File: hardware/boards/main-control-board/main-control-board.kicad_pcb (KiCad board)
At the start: 2 copper layers, 122.9 x 33 mm, 7 parts, among them J1 Conn_MAX98357, J2 Conn_OLED, J3 Conn_PCA9685_1, J4 Conn_PCA9685_2, J5 Conn_ESP32_R, J6 Conn_ESP32_L, J7 Conn_USB

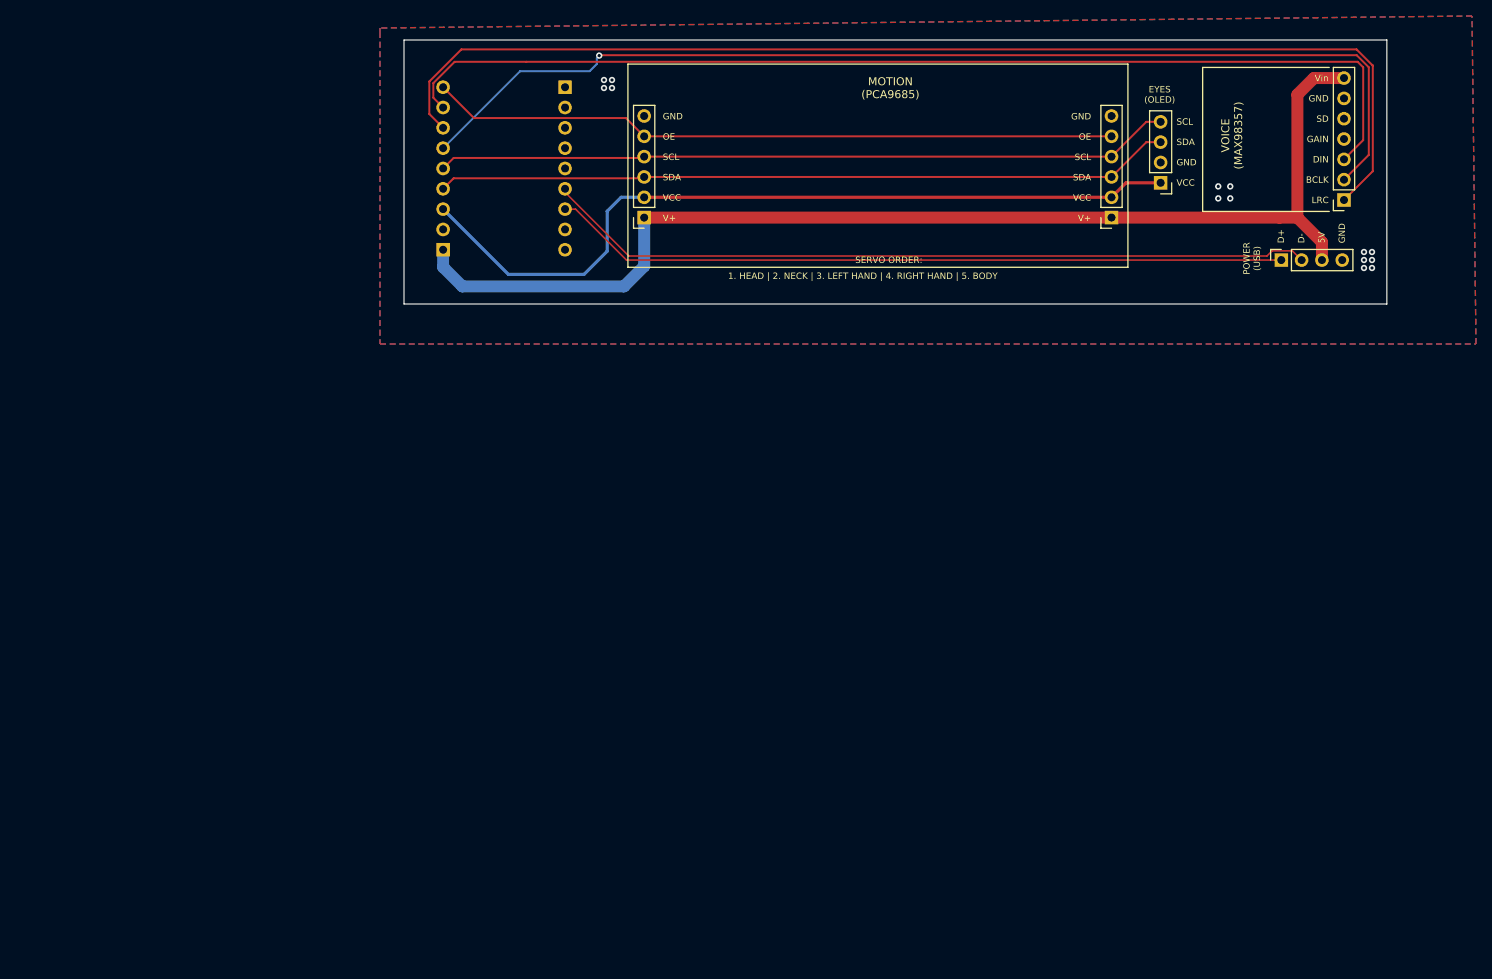
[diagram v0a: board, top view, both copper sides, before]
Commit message: reshape the board to mount SDM USB
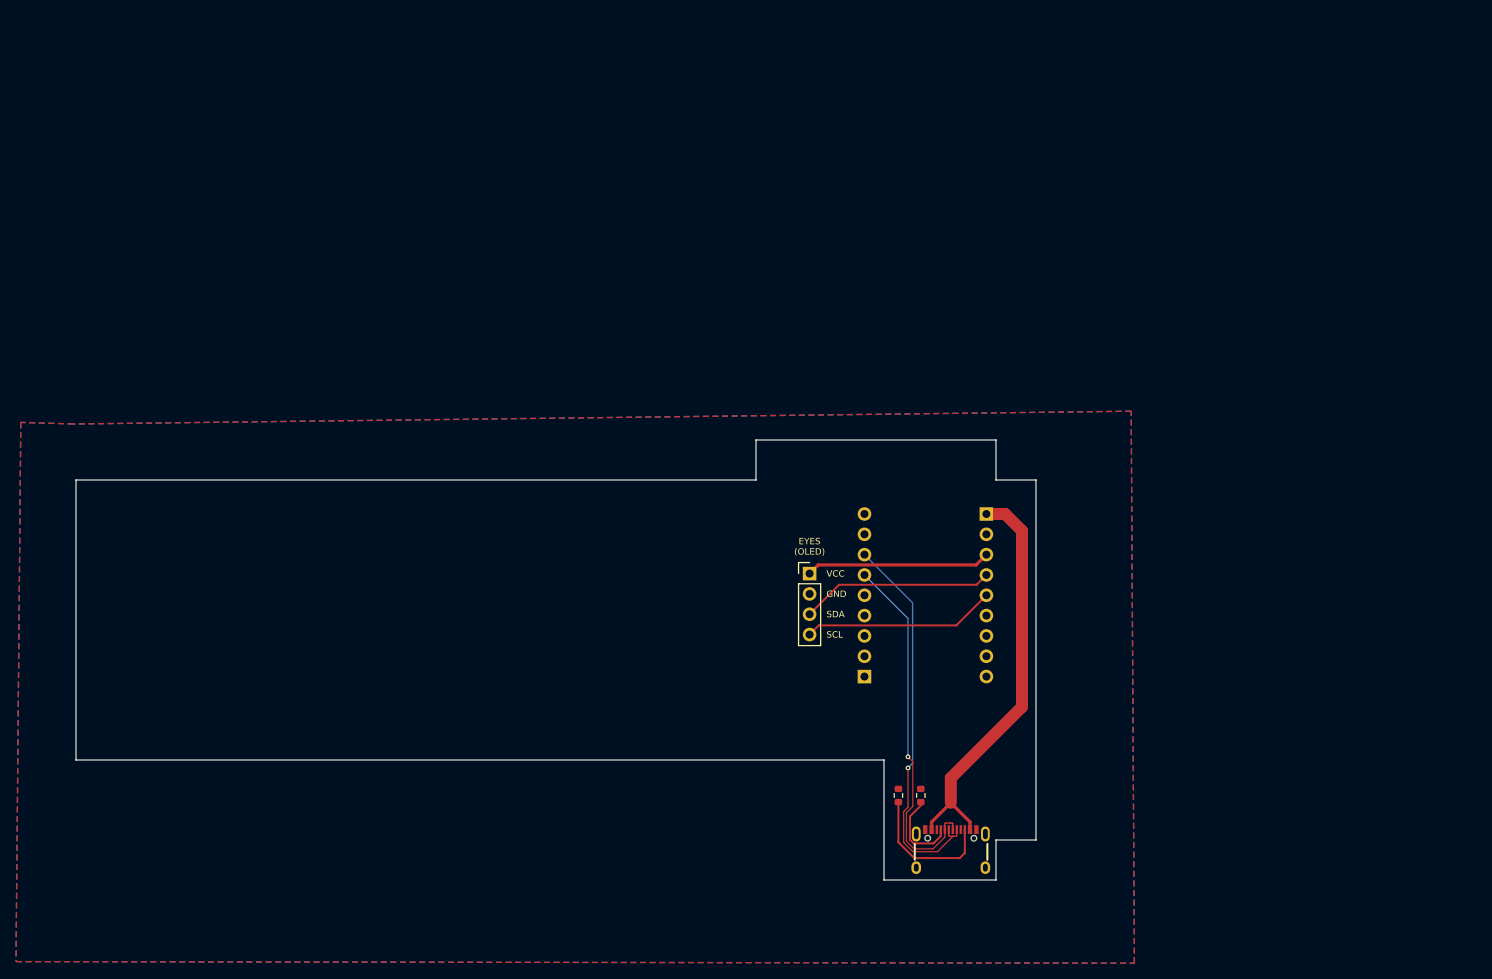
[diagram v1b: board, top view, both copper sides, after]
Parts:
- removed J1: Conn_MAX98357, Connector_PinSocket_2.54mm:PinSocket_1x07_P2.54mm_Vertical
- removed J3: Conn_PCA9685_1, Connector_PinSocket_2.54mm:PinSocket_1x06_P2.54mm_Vertical
- removed J4: Conn_PCA9685_2, Connector_PinSocket_2.54mm:PinSocket_1x06_P2.54mm_Vertical
- removed J7: Conn_USB, Connector_PinSocket_2.54mm:PinSocket_1x04_P2.54mm_Vertical
- added R1: 5.1k, Resistor_SMD:R_0603_1608Metric, F.Cu at (188.1, 124.4)
- added R2: 5.1k, Resistor_SMD:R_0603_1608Metric, F.Cu at (185.3, 124.4)
- added USB1: TYPE-C 16PIN 2MD, easyeda:USB-C-SMD_TYPE-C-16PIN-2MD-073, F.Cu at (191.8, 131.1)
- moved J5 82.6 mm to (181.1, 109.6), turned to 0 degrees
- moved J6 75.5 mm to (196.3, 89.2), turned to 180 degrees
- moved J2 65.7 mm to (174.2, 96.7), turned to 0 degrees
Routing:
- net /I2S_LRC: track 145.2 -> 0.00 mm
- net /I2S_BCLK: track 136.9 -> 0.00 mm, vias 1 -> 0
- net /I2S_DIN: track 133.7 -> 0.00 mm
- net +5V: track 145.7 -> 51.7 mm
- net Net-(J3-Pin_5): track 86.1 -> 0.00 mm
- net +3.3V: track 101.0 -> 23.1 mm
- net /I2C_SCL: track 92.2 -> 24.1 mm
- net /I2C_SDA: track 92.1 -> 24.1 mm
- net /USB_D-: track 96.5 -> 45.4 mm, vias 0 -> 1
- net /USB_D+: track 92.2 -> 48.9 mm, vias 0 -> 1
- net Net-(USB1-CC2): track 0.00 -> 17.3 mm
- net Net-(USB1-CC1): track 0.00 -> 10.5 mm
- net GND: vias 14 -> 0
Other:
- board size 122.9 x 33 mm -> 120 x 55 mm
- board text removed: "1. HEAD | 2. NECK | 3. LEFT HAND | 4. RIGHT HAND | 5. BODY"
- board text removed: "BCLK"
- board text removed: "D+"
- board text removed: "D-"
- board text removed: "DIN"
- board text removed: "GAIN"
- board text removed: "LRC"
- board text removed: "MOTION (PCA9685)"
- board text removed: "OE"
- board text removed: "POWER (USB)"
- board text removed: "SD"
- board text removed: "SERVO ORDER:"
- board text removed: "V+"
- board text removed: "VOICE (MAX98357)"
- board text removed: "Vin"

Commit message: use hierarchical sheets in schmatic
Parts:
- removed J5: Conn_ESP32_R, Connector_PinSocket_2.54mm:PinSocket_1x09_P2.54mm_Vertical
- removed J6: Conn_ESP32_L, Connector_PinSocket_2.54mm:PinSocket_1x09_P2.54mm_Vertical
- added J7: Conn_ESP32_L, Connector_PinSocket_2.54mm:PinSocket_1x09_P2.54mm_Vertical, B.Cu at (196.3, 89.3)
- added J8: Conn_ESP32_R, Connector_PinSocket_2.54mm:PinSocket_1x09_P2.54mm_Vertical, B.Cu at (181.1, 109.6)
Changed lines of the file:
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@@
 			)
 		)
-		(sheetname "/")
-		(sheetfile "main-control-board.kicad_sch")
+		(sheetname "/USB/")
+		(sheetfile "main-control-board-usb.kicad_sch")
+		(units
+			(unit
+				(name "A")
+				(pins "A1B12" "A4B9" "B8" "A5" "B7" "A6" "A7" "B6" "A8" "B5" "B4A9" "B1A12"
+					"13" "14"
+				)
+			)
+		)
 		(attr smd)
 		(duplicate_pad_numbers_are_jumpers no)
@@
 			)
 		)
-		(property "KiLib_Generator" "SMD_2terminal_chip_molded"
-			(at 0 0 90)
-			(layer "F.SilkS")
-			(hide yes)
-			(effects
-				(font
-					(size 1 1)
-					(thickness 0.15)
-				)
-			)
-		)
 		(property "LCSC Part #" "C23186"
 			(at 0 0 270)
@@
 		)
 		(property ki_fp_filters "R_*")
-		(sheetname "/")
-		(sheetfile "main-control-board.kicad_sch")
+		(sheetname "/USB/")
+		(sheetfile "main-control-board-usb.kicad_sch")
 		(units
 			(unit
@@
 			)
 		)
-		(property "KiLib_Generator" "SMD_2terminal_chip_molded"
-			(at 0 0 90)
-			(layer "F.SilkS")
-			(hide yes)
-			(effects
-				(font
-					(size 1 1)
-					(thickness 0.15)
-				)
-			)
-		)
 		(property "LCSC Part #" "C23186"
 			(at 0 0 270)
@@
 		)
 		(property ki_fp_filters "R_*")
-		(sheetname "/")
-		(sheetfile "main-control-board.kicad_sch")
+		(sheetname "/USB/")
+		(sheetfile "main-control-board-usb.kicad_sch")
 		(units
 			(unit
@@
 	)
 	(footprint "Connector_PinSocket_2.54mm:PinSocket_1x09_P2.54mm_Vertical"
+		(locked yes)
 		(layer "B.Cu")
-		(at 196.3 89.25 180)
+		(at 196.3 89.28 180)
 		(descr "Through hole straight socket strip, 1x09, 2.54mm pitch, single row (from Kicad 4.0.7), script generated")
 		(tags "Through hole socket strip THT 1x09 2.54mm single row")
-		(property "Reference" "J6"
+		(property "Reference" "J7"
 			(at 0 2.77 0)
 			(layer "B.SilkS")
@@
 			(at 0 -23.09 0)
 			(layer "B.Fab")
-			(hide yes)
 			(effects
 				(font
@@
 				(font
 					(size 1.27 1.27)
-				)
-				(justify mirror)
-			)
-		)
-		(property "KiLib_Generator" "connector/pin_header_socket"
-			(at 0 0 0)
-			(layer "B.SilkS")
-			(hide yes)
-			(effects
-				(font
-					(size 1 1)
-					(thickness 0.15)
 				)
 				(justify mirror)
@@
 		)
 		(property ki_fp_filters "Connector*:*_1x??_*")
-		(sheetname "/")
-		(sheetfile "main-control-board.kicad_sch")
+		(sheetname "/ESP32/")
+		(sheetfile "main-control-board-esp32.kicad_sch")
 		(units
 			(unit
@@
 			(layers "*.Cu" "*.Mask")
 			(remove_unused_layers no)
-			(net "Net-(J3-Pin_5)")
+			(net "/ESP32/GP5")
 			(pinfunction "Pin_9_9")
 			(pintype "passive")
@@
 	)
 	(footprint "Connector_PinSocket_2.54mm:PinSocket_1x09_P2.54mm_Vertical"
+		(locked yes)
 		(layer "B.Cu")
-		(at 181.06 109.57)
+		(at 181.06 109.6)
 		(descr "Through hole straight socket strip, 1x09, 2.54mm pitch, single row (from Kicad 4.0.7), script generated")
 		(tags "Through hole socket strip THT 1x09 2.54mm single row")
-		(property "Reference" "J5"
+		(property "Reference" "J8"
 			(at 0 2.77 0)
 			(layer "B.SilkS")
@@
 			(at 0 -23.09 0)
 			(layer "B.Fab")
-			(hide yes)
 			(effects
 				(font
@@
 				(font
 					(size 1.27 1.27)
-				)
-				(justify mirror)
-			)
-		)
-		(property "KiLib_Generator" "connector/pin_header_socket"
-			(at 0 0 0)
-			(layer "B.SilkS")
-			(hide yes)
-			(effects
-				(font
-					(size 1 1)
-					(thickness 0.15)
 				)
 				(justify mirror)
@@
 		)
 		(property ki_fp_filters "Connector*:*_1x??_*")
-		(sheetname "/")
-		(sheetfile "main-control-board.kicad_sch")
+		(sheetname "/ESP32/")
+		(sheetfile "main-control-board-esp32.kicad_sch")
 		(units
 			(unit
@@
 			(layers "*.Cu" "*.Mask")
 			(remove_unused_layers no)
-			(net "Net-(J5-Pin_1)")
+			(net "Net-(J8-Pin_1)")
 			(pinfunction "Pin_1_1")
 			(pintype "passive")
@@
 			(layers "*.Cu" "*.Mask")
 			(remove_unused_layers no)
-			(net "Net-(J5-Pin_2)")
+			(net "Net-(J8-Pin_2)")
 			(pinfunction "Pin_2_2")
 			(pintype "passive")
@@
 			(layers "*.Cu" "*.Mask")
 			(remove_unused_layers no)
-			(net "Net-(J5-Pin_3)")
+			(net "Net-(J8-Pin_3)")
 			(pinfunction "Pin_3_3")
 			(pintype "passive")
@@
 			(layers "*.Cu" "*.Mask")
 			(remove_unused_layers no)
-			(net "Net-(J5-Pin_4)")
+			(net "Net-(J8-Pin_4)")
 			(pinfunction "Pin_4_4")
 			(pintype "passive")
@@
 			(layers "*.Cu" "*.Mask")
 			(remove_unused_layers no)
-			(net "Net-(J5-Pin_5)")
+			(net "Net-(J8-Pin_5)")
 			(pinfunction "Pin_5_5")
 			(pintype "passive")
@@
 			(layers "*.Cu" "*.Mask")
 			(remove_unused_layers no)
-			(net "Net-(J5-Pin_8)")
+			(net "Net-(J8-Pin_8)")
 			(pinfunction "Pin_8_8")
 			(pintype "passive")
@@
 			(layers "*.Cu" "*.Mask")
 			(remove_unused_layers no)
-			(net "Net-(J5-Pin_9)")
+			(net "Net-(J8-Pin_9)")
 			(pinfunction "Pin_9_9")
 			(pintype "passive")
@@
 	)
 	(segment
-		(start 196.3 94.33)
-		(end 195.01 95.62)
+		(start 195.05 95.61)
+		(end 196.3 94.36)
 		(width 0.4)
 		(layer "F.Cu")
@@
 	)
 	(segment
-		(start 175.28 95.62)
-		(end 174.2 96.7)
+		(start 175.29 95.61)
+		(end 195.05 95.61)
 		(width 0.4)
 		(layer "F.Cu")
@@
 	)
 	(segment
-		(start 195.01 95.62)
-		(end 175.28 95.62)
+		(start 174.2 96.7)
+		(end 175.29 95.61)
 		(width 0.4)
 		(layer "F.Cu")
@@
 	)
 	(segment
-		(start 177.885 98.095)
-		(end 174.2 101.78)
+		(start 175.225 100.755)
+		(end 192.445 100.755)
 		(width 0.25)
 		(layer "F.Cu")
@@
 	)
 	(segment
-		(start 195.075 98.095)
-		(end 177.885 98.095)
+		(start 174.2 101.78)
+		(end 175.225 100.755)
 		(width 0.25)
 		(layer "F.Cu")
@@
 	)
 	(segment
-		(start 196.3 96.87)
-		(end 195.075 98.095)
+		(start 192.445 100.755)
+		(end 196.3 96.9)
 		(width 0.25)
 		(layer "F.Cu")
@@
 	)
 	(segment
-		(start 192.535 103.175)
-		(end 175.345 103.175)
+		(start 174.2 104.32)
+		(end 175.225 103.295)
 		(width 0.25)
 		(layer "F.Cu")
@@
 	)
 	(segment
-		(start 175.345 103.175)
-		(end 174.2 104.32)
+		(start 192.445 103.295)
+		(end 196.3 99.44)
 		(width 0.25)
 		(layer "F.Cu")
@@
 	)
 	(segment
-		(start 196.3 99.41)
-		(end 192.535 103.175)
+		(start 175.225 103.295)
+		(end 192.445 103.295)
 		(width 0.25)
 		(layer "F.Cu")
@@
 	)
 	(segment
-		(start 187.075 120.425)
-		(end 187.075 100.345)
+		(start 186.5 121)
+		(end 187.075 120.425)
 		(width 0.15)
 		(layer "B.Cu")
@@
 	)
 	(segment
-		(start 187.075 100.345)
-		(end 181.06 94.33)
+		(start 187.075 120.425)
+		(end 187.075 100.375)
 		(width 0.15)
 		(layer "B.Cu")
@@
 	)
 	(segment
-		(start 186.5 121)
-		(end 187.075 120.425)
+		(start 187.075 100.375)
+		(end 181.06 94.36)
 		(width 0.15)
 		(layer "B.Cu")
@@
 	(segment
 		(start 186.5 119.6)
-		(end 186.5 102.31)
+		(end 186.5 102.34)
 		(width 0.15)
 		(layer "B.Cu")
@@
 	)
 	(segment
-		(start 186.5 102.31)
-		(end 181.06 96.87)
+		(start 186.5 102.34)
+		(end 181.06 96.9)
 		(width 0.15)
 		(layer "B.Cu")
@@
 	(group ""
 		(locked yes)
-		(members "2cac99a0-514c-4601-805a-e1ec277969cc" "f2f5e2be-bc17-434f-a69a-85fb81988b96")
+		(members "449babe4-efb9-4fae-a58a-771fc8d23471" "4ad19bc7-25f0-4f5a-8fad-488d811bb7ef")
 	)
 	(group ""
-		(locked yes)
-		(members "0239887b-eb8f-45e6-9ae8-d63ca8a7e710" "219d5843-0b81-410b-87a3-158a1eddf31c"
-			"221b42d0-965b-4419-a00e-0f987fd2e50b" "352a9a0b-81da-40a7-828a-07fc1659d33d"
-			"357912f4-084d-43a9-97c0-64e3dbea975d" "39daa80d-c9c6-4168-b1fa-b7927e1fffef"
-			"3b2bc2ac-bb8f-488e-81c9-c42934a201b9" "44fc8eb7-8f76-4fa2-954f-092751f93c75"
-			"5b8532a1-ced0-4a0e-9e42-351476e8918b" "637a7e1b-f6a4-4efa-af3c-16027cbf096f"
-			"6afcfd97-11d3-49cd-b673-499d03f2c0ed" "78a27f02-406b-4304-8a22-4756b9b6f811"
-			"832ecbdc-d134-44ff-8689-0e1dbe0cb93a" "89a9517f-202e-4dde-9ed7-d0a3a02fd3f2"
-			"a87f910d-791f-4880-95c9-6ec2022a24f1" "aa43e353-9b68-4459-94c6-60542ca405eb"
-			"b60553d6-3779-48f0-bb07-2f07a1fad4a5" "bb242292-5098-4d9c-8472-5263c2347eb8"
-			"bb6781a5-a259-413c-8402-1f547eb60e79" "c255b7c8-d3db-4d3b-bfd1-9f4135fca439"
-			"cae9c790-ef36-4d7c-9702-5b7bb861f9d1" "cdf25b00-a169-46c5-a45d-d59eab11a39f"
-			"d3fae790-f8f5-4272-bc32-43641e4ea027" "e2324006-1ee4-4513-a3d4-50a4535c0018"
-			"f42ad876-2563-4b4f-8ca8-533c6ff48653" "fbc69c1e-dcfb-47b2-9f20-70c36592a2ab"
-		)
-	)
-	(group ""

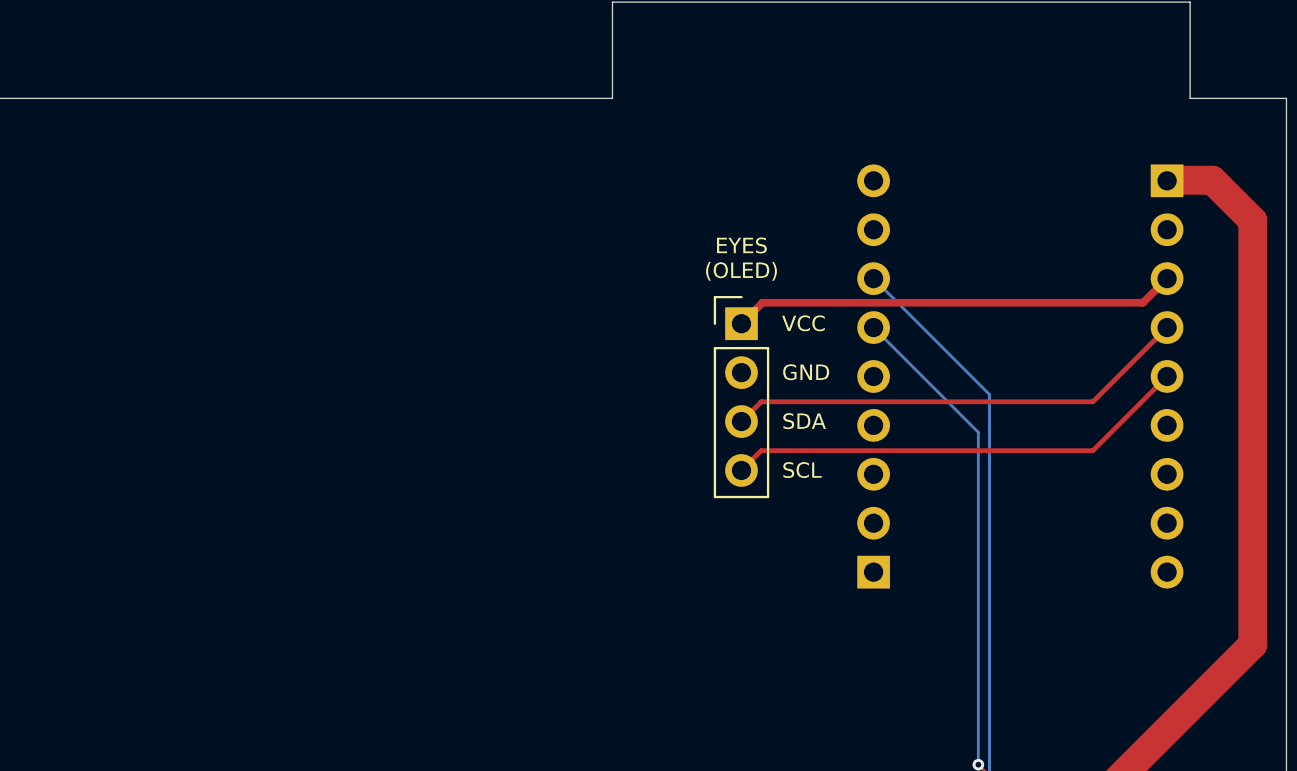
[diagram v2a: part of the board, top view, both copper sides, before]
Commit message: integrate PCA into the board
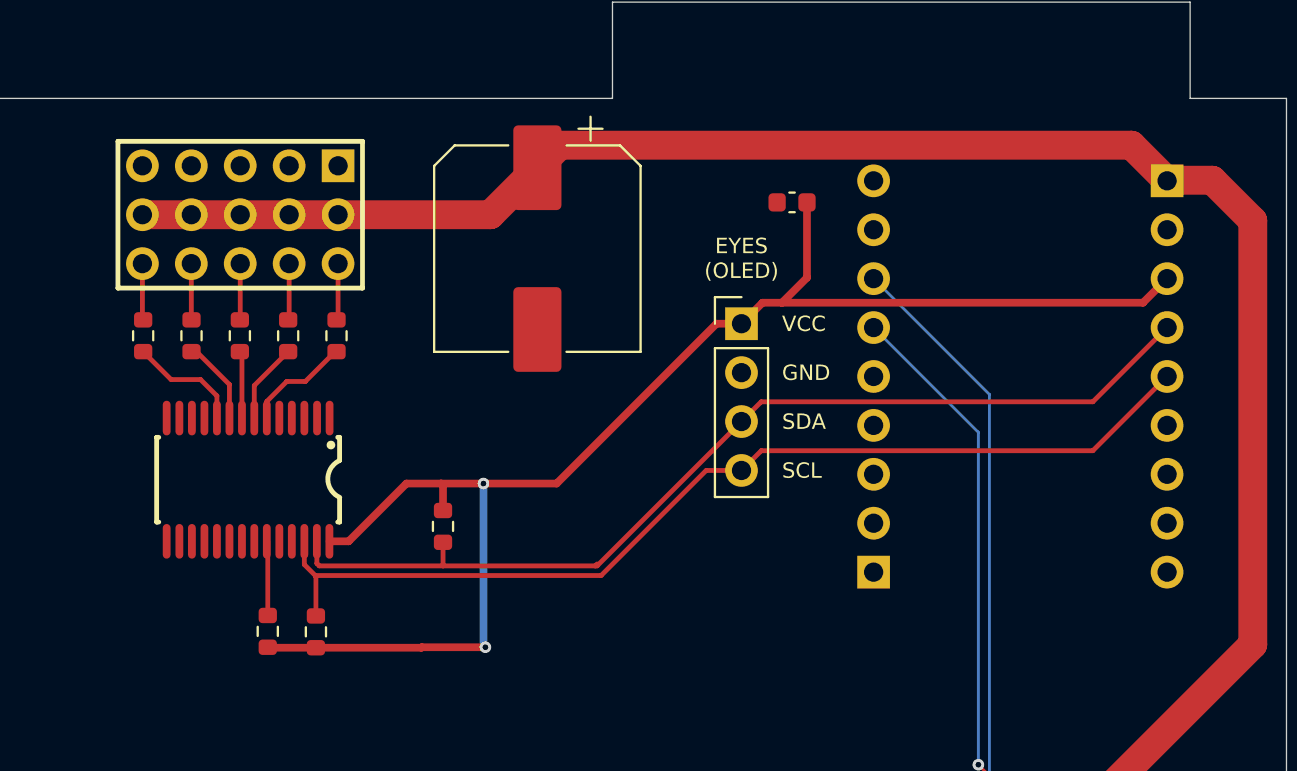
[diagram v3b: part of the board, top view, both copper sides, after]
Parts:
- added C1: 100nF, Capacitor_SMD:C_0603_1608Metric, F.Cu at (176.8, 90.4)
- added C2: 1000uF, Capacitor_SMD:CP_Elec_10x10.5, F.Cu at (163.6, 92.8)
- added R10: 220, Resistor_SMD:R_0603_1608Metric, F.Cu at (143.1, 97.3)
- added R3: 10k, Resistor_SMD:R_0603_1608Metric, F.Cu at (149.6, 112.7)
- added R4: 4.7k, Resistor_SMD:R_0603_1608Metric, F.Cu at (152.1, 112.7)
- added R5: 4.7k, Resistor_SMD:R_0603_1608Metric, F.Cu at (158.7, 107.2)
- added R6: 220, Resistor_SMD:R_0603_1608Metric, F.Cu at (153.2, 97.3)
- added R7: 220, Resistor_SMD:R_0603_1608Metric, F.Cu at (150.7, 97.3)
- added R8: 220, Resistor_SMD:R_0603_1608Metric, F.Cu at (148.2, 97.3)
- added R9: 220, Resistor_SMD:R_0603_1608Metric, F.Cu at (145.6, 97.3)
- added U1: PCA9685PW,118, easyeda:TSSOP-28_L9.7-W4.4-P0.65-LS6.4-TL, F.Cu at (148.6, 104.8)
- added U2: HX PZ2.54-3X5P ZZ, easyeda:HDR-TH_15P-P2.54-V-M-R3-C5-S7.5, F.Cu at (148.2, 91.0)
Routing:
- net +5V: track 51.7 -> 107.2 mm
- net +3.3V: track 23.1 -> 76.9 mm, vias 0 -> 2
- net /I2C_SCL: track 24.1 -> 52.6 mm
- net /I2C_SDA: track 24.1 -> 51.8 mm
- net Net-(U1-LED4): track 0.00 -> 5.93 mm
- net Net-(U1-LED0): track 0.00 -> 5.56 mm
- net Net-(U1-LED3): track 0.00 -> 4.42 mm
- net Net-(U1-LED1): track 0.00 -> 4.18 mm
- net /ESP32/GP5: track 0.00 -> 3.87 mm
- net Net-(U1-LED2): track 0.00 -> 3.50 mm
- net Net-(R6-Pad2): track 0.00 -> 2.95 mm
- net Net-(R7-Pad2): track 0.00 -> 2.94 mm
- net Net-(R10-Pad2): track 0.00 -> 2.94 mm
- net Net-(R8-Pad2): track 0.00 -> 2.93 mm
- net Net-(R9-Pad2): track 0.00 -> 2.92 mm
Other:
- board text added: "Main Control Board REV #2 | 2026-09-22 github.com/jamro/tiny-engineer"
- board text removed: "Main Control Board REV #1 | 2026-09-12 github.com/jamro/tiny-engineer"

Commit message: add power indicator
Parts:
- added D1: LED, LED_SMD:LED_0603_1608Metric, F.Cu at (195.8, 124.2)
- added R11: 2.2k, Resistor_SMD:R_0603_1608Metric, F.Cu at (198.3, 124.2)
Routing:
- net +5V: track 107.2 -> 116.9 mm
- net Net-(D1-A): track 0.00 -> 2.58 mm
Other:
- board text added: "POWER"
